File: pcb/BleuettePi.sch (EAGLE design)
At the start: 102 parts, among them IC1 PIC18F452, IC2 DS1339, IC3 MAX4173FESA+, IC5 MCP23017SS, IC6 LM386M-1, IC7 GY-27, Q1 10Mhz

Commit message: First Python code
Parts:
- added D2: 3V3, diode:ZENER-DIODESOT23
- C1, C2: value (none) -> 470uf
- C12, C16, C6: value (none) -> 100nf
- C13: value (none) -> 4.7uf; device rcl:CPOL-EUA -> rcl:CPOL-EUCT3528
- C14, C15: device rcl:CPOL-EUA -> rcl:CPOL-EUCT3528
- C20: value (none) -> 10uf; device rcl:CPOL-EUA -> rcl:CPOL-EUCT3528
- C9: value (none) -> 100uf
- IC2: value DS1339 -> DS1307
- Q6: value (none) -> 32.768KHz
- R19: value 10 -> 1k
- S0, S1, S10, S11, S2, S3, S4, S5, S6, S7, S8, S9, SX, SY: value (none) -> CONN_SERVO; device con-lstb:MA03-1 -> bleuette:CONN_SERVO
- renumbered D3 to D1
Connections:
- net +5V: now also SPLY-1.KL; no longer SPLY-3.KL
- net +7V: now also SPLY-3.KL; no longer SPLY-1.KL
- net N$19: now also SX.S; no longer SX.3
- net N$24: now also SY.S; no longer SY.3
- net N$58: now also CR1220.+1; no longer CR1220.-
- net RX_PI: now also D2.C
- net SS0: now also S0.S; no longer S0.3
- net SS1: now also S1.S; no longer S1.3
- net SS10: now also S10.S; no longer S10.3
- net SS11: now also S11.S; no longer S11.3
- net SS2: now also S2.S; no longer S2.3
- net SS3: now also S3.S; no longer S3.3
- net SS4: now also S4.S; no longer S4.3
- net SS5: now also S5.S; no longer S5.3
- net SS6: now also S6.S; no longer S6.3
- net SS7: now also S7.S; no longer S7.3
- net SS8: now also S8.S; no longer S8.3
- net SS9: now also S9.S; no longer S9.3
- net VEE: now also S0.+, S1.+, S10.+, S11.+, S2.+, S3.+, S4.+, S5.+, S6.+, S7.+, S8.+, S9.+, SX.+, SY.+; no longer S0.2, S1.2, S10.2, S11.2, S2.2, S3.2, S4.2, S5.2, S6.2, S7.2, S8.2, S9.2, SX.2, SY.2
- net VSS: now also CR1220.-, D2.A, S0.-, S1.-, S10.-, S11.-, S2.-, S3.-, S4.-, S5.-, S6.-, S7.-, S8.-, S9.-, SX.-, SY.-; no longer CR1220.+, CR1220.+1, S0.1, S1.1, S10.1, S11.1, S2.1, S3.1, S4.1, S5.1, S6.1, S7.1, S8.1, S9.1, SX.1, SY.1
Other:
- moved on the sheet: C30, C31, CR1220, R10, R9, SPLY-1, SPLY-3

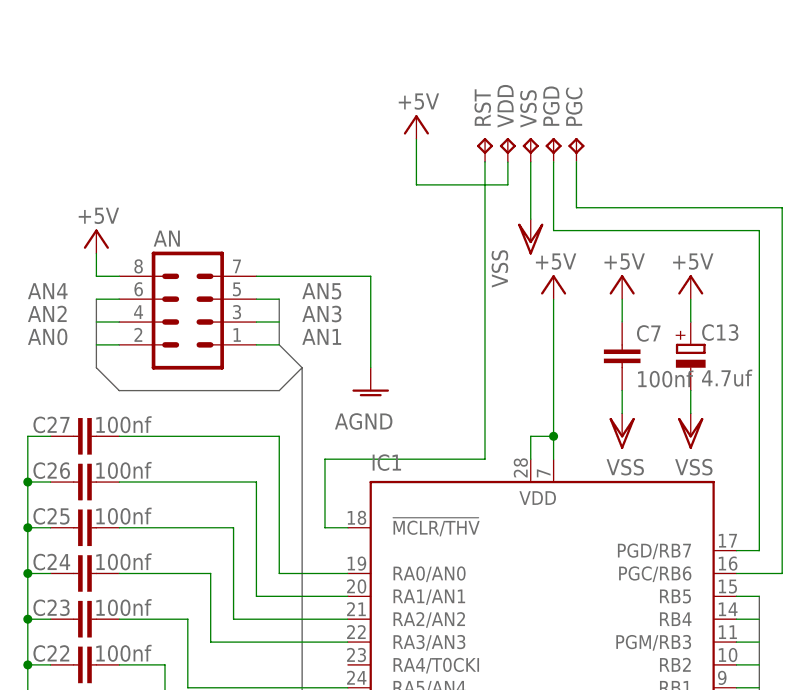
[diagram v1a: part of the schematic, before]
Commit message: Added R4, MCLR pullup
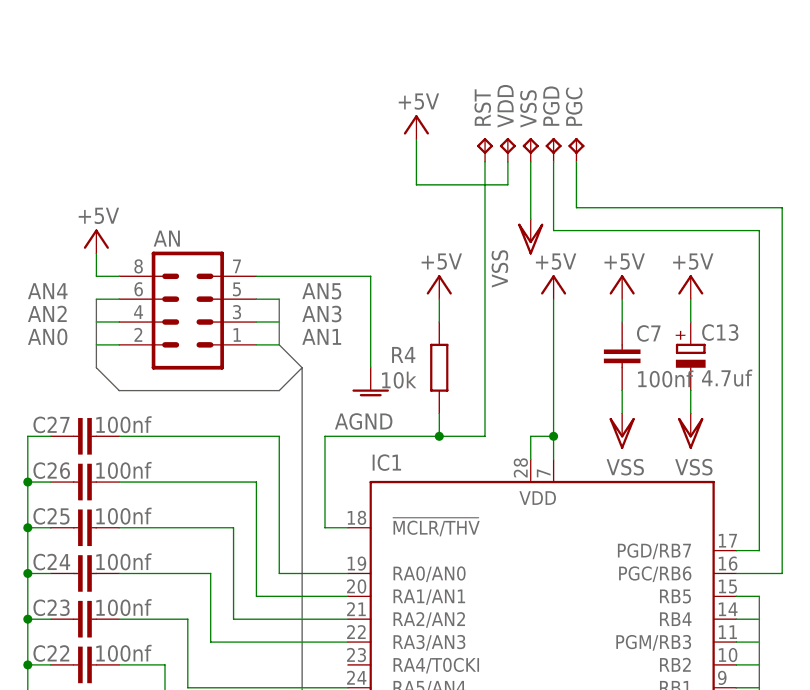
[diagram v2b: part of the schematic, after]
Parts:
- added R4: 10k, rcl:R-EU_M0805
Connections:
- net N$16 renamed TX_PIC
- net +5V: now also R4.2
- net UC_RESET: now also R4.1
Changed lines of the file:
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@@
 <part name="C20" library="rcl" deviceset="CPOL-EU" device="CT3528" value="10uf"/>
 <part name="C13" library="rcl" deviceset="CPOL-EU" device="CT3528" value="4.7uf"/>
+<part name="R4" library="rcl" deviceset="R-EU_" device="M0805" value="10k"/>
+<part name="P+21" library="supply1" deviceset="+5V" device=""/>
 </parts>
 <sheets>
@@
 <instance part="C20" gate="G$1" x="360.68" y="116.84"/>
 <instance part="C13" gate="G$1" x="106.68" y="109.22"/>
+<instance part="R4" gate="G$1" x="78.74" y="106.68" smashed="yes" rot="R90">
+<attribute name="NAME" x="76.2" y="108.9914" size="1.778" layer="95" rot="R180"/>
+<attribute name="VALUE" x="76.2" y="106.172" size="1.778" layer="96" rot="R180"/>
+</instance>
+<instance part="P+21" gate="1" x="78.74" y="116.84" smashed="yes">
+<attribute name="VALUE" x="81.28" y="119.38" size="1.778" layer="96" rot="R180"/>
+</instance>
 </instances>
 <busses>
@@
 <wire x1="66.04" y1="228.6" x2="66.04" y2="231.14" width="0.1524" layer="91"/>
 </segment>
+<segment>
+<pinref part="R4" gate="G$1" pin="2"/>
+<pinref part="P+21" gate="1" pin="+5V"/>
+<wire x1="78.74" y1="114.3" x2="78.74" y2="111.76" width="0.1524" layer="91"/>
+</segment>
 </net>
 <net name="VDD" class="0">
@@
 <segment>
 <wire x1="68.58" y1="88.9" x2="66.04" y2="88.9" width="0.1524" layer="91"/>
-<wire x1="66.04" y1="88.9" x2="66.04" y2="96.52" width="0.1524" layer="91"/>
-<wire x1="83.82" y1="96.52" x2="83.82" y2="129.54" width="0.1524" layer="91"/>
-<wire x1="66.04" y1="96.52" x2="83.82" y2="96.52" width="0.1524" layer="91"/>
+<wire x1="66.04" y1="88.9" x2="66.04" y2="99.06" width="0.1524" layer="91"/>
+<wire x1="83.82" y1="99.06" x2="83.82" y2="129.54" width="0.1524" layer="91"/>
+<wire x1="66.04" y1="99.06" x2="78.74" y2="99.06" width="0.1524" layer="91"/>
 <pinref part="IC1" gate="G$1" pin="!MCLR/THV"/>
 <pinref part="RST" gate="G$1" pin="TP"/>
+<pinref part="R4" gate="G$1" pin="1"/>
+<wire x1="78.74" y1="99.06" x2="83.82" y2="99.06" width="0.1524" layer="91"/>
+<wire x1="78.74" y1="101.6" x2="78.74" y2="99.06" width="0.1524" layer="91"/>
+<junction x="78.74" y="99.06"/>
 </segment>
 </net>
@@
 </segment>
 </net>
-<net name="N$16" class="0">
+<net name="TX_PIC" class="0">
 <segment>
 <pinref part="IC1" gate="G$1" pin="TX/RC6"/>

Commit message: Modif PCB
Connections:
- net N$1 renamed RC1
- net N$2 renamed RC2
- net N$3 renamed RC3
- net N$55 renamed RC4
- net N$56 renamed RC5
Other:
- note added: "Ajouter un Vref+ / Vref-"
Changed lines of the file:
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@@
 <wire x1="290.83" y1="93.98" x2="283.21" y2="93.98" width="0.1524" layer="98" style="shortdash"/>
 <text x="276.86" y="135.89" size="1.778" layer="98">One of them</text>
+<text x="71.12" y="266.7" size="2.54" layer="98">Ajouter un Vref+ / Vref-</text>
 </plain>
 <instances>
@@
 </segment>
 </net>
-<net name="N$55" class="0">
+<net name="RC4" class="0">
 <segment>
 <pinref part="IC1" gate="G$1" pin="SDI/RC4"/>
@@
 </segment>
 </net>
-<net name="N$56" class="0">
+<net name="RC5" class="0">
 <segment>
 <pinref part="IC1" gate="G$1" pin="SDO/RC5"/>
@@
 </segment>
 </net>
-<net name="N$1" class="0">
+<net name="RC1" class="0">
 <segment>
 <pinref part="IC1" gate="G$1" pin="RC1/T1OSI"/>
@@
 </segment>
 </net>
-<net name="N$2" class="0">
+<net name="RC2" class="0">
 <segment>
 <pinref part="IC1" gate="G$1" pin="RC2/CCP1"/>
@@
 </segment>
 </net>
-<net name="N$3" class="0">
+<net name="RC3" class="0">
 <segment>
 <pinref part="IC1" gate="G$1" pin="RC3/SCK"/>

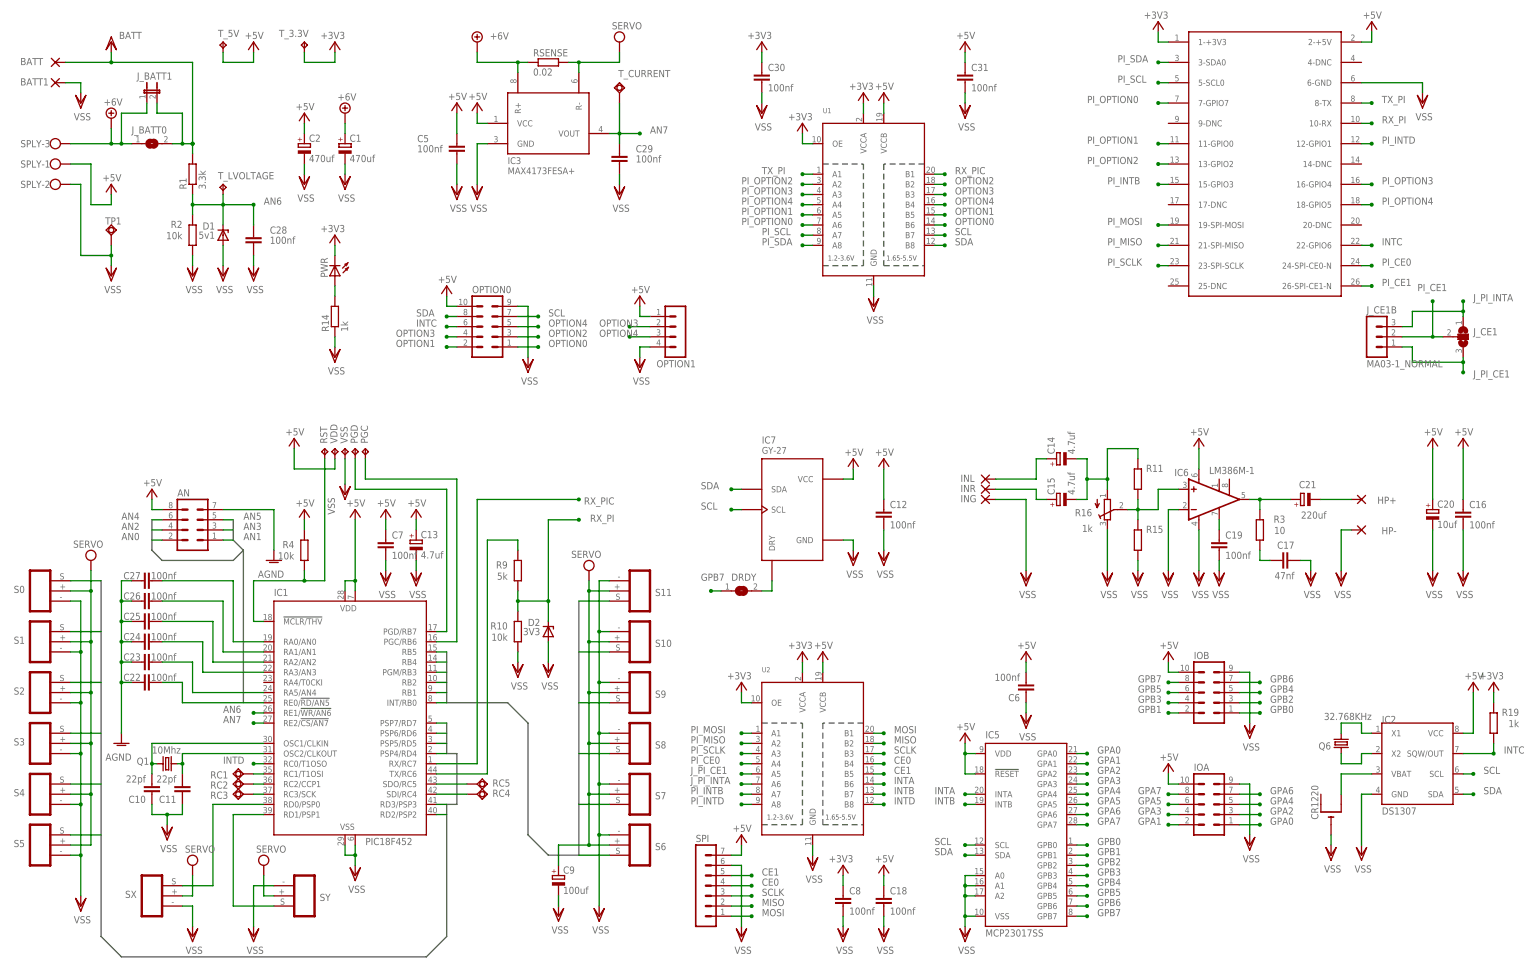
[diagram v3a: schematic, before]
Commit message: I2C linked to Pic + Misc
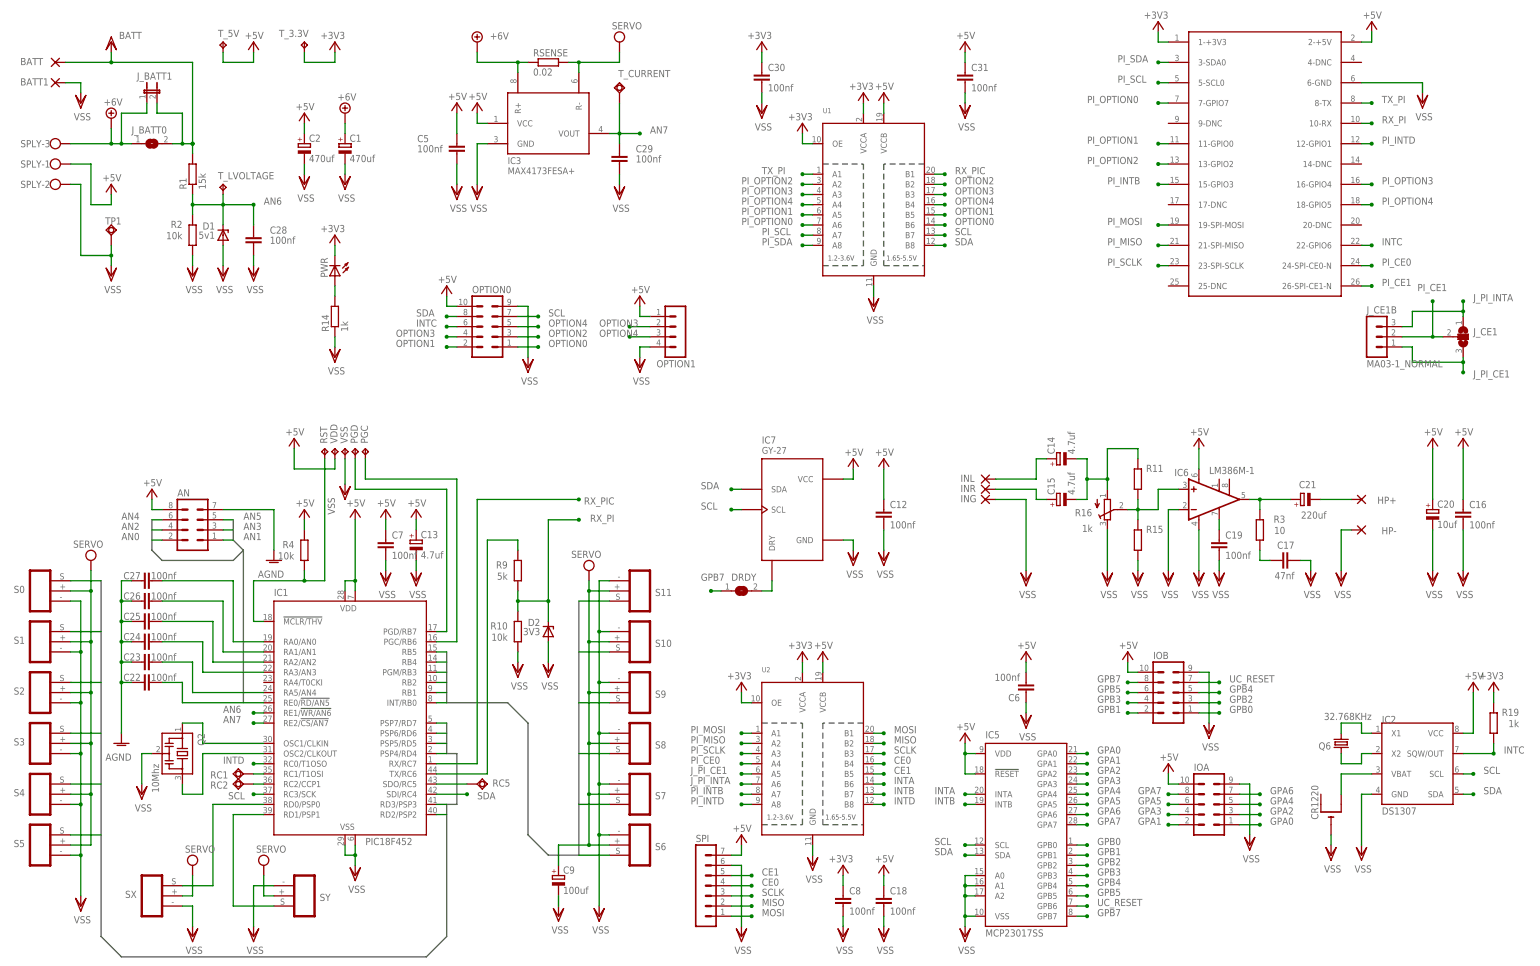
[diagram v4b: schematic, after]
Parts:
- removed C10, C11: 22pf, rcl:C-EUC0805
- removed Q1: 10Mhz, crystal:CRYTALHC49UP
- removed RC3, RC4: TPSQTP06SQ, testpad:TPSQTP06SQ
- added Q2: 10Mhz, murata-filter:CSTCR6M00G53Z
- R1: value 3.3k -> 15k
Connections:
- removed net GPB6: IC5.GPB6, IOB.7
- removed net N$25: C11.2, IC1.OSC2/CLKOUT, Q1.1
- removed net N$27: C10.2, IC1.OSC1/CLKIN, Q1.2
- removed net RC3: IC1.RC3/SCK, RC3.TP
- removed net RC4: IC1.SDI/RC4, RC4.TP
- new net N$1: IC1.OSC2/CLKOUT, Q2.3
- new net N$2: IC1.OSC1/CLKIN, Q2.1
- net SCL: now also IC1.RC3/SCK
- net SDA: now also IC1.SDI/RC4
- net UC_RESET: now also IC5.GPB6, IOB.7
- net VSS: now also Q2.2; no longer C10.1, C11.1
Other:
- note added: "GPB6: Pic Reset"
- note added: "GPB7: GY-27 DRDY"
- note added: "R1/R2 value for 12v battery"
- moved on the sheet: IOB
